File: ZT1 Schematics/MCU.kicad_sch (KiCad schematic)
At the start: 23 parts, among them SW101 PB_WPTKT, U103 74LS02, U106 74LS32, U107 74LS08, U108 74LS00, U111 D444C, U113 2732, U114 2732, U117 P8031AH, U118 74LS373, U127 7432

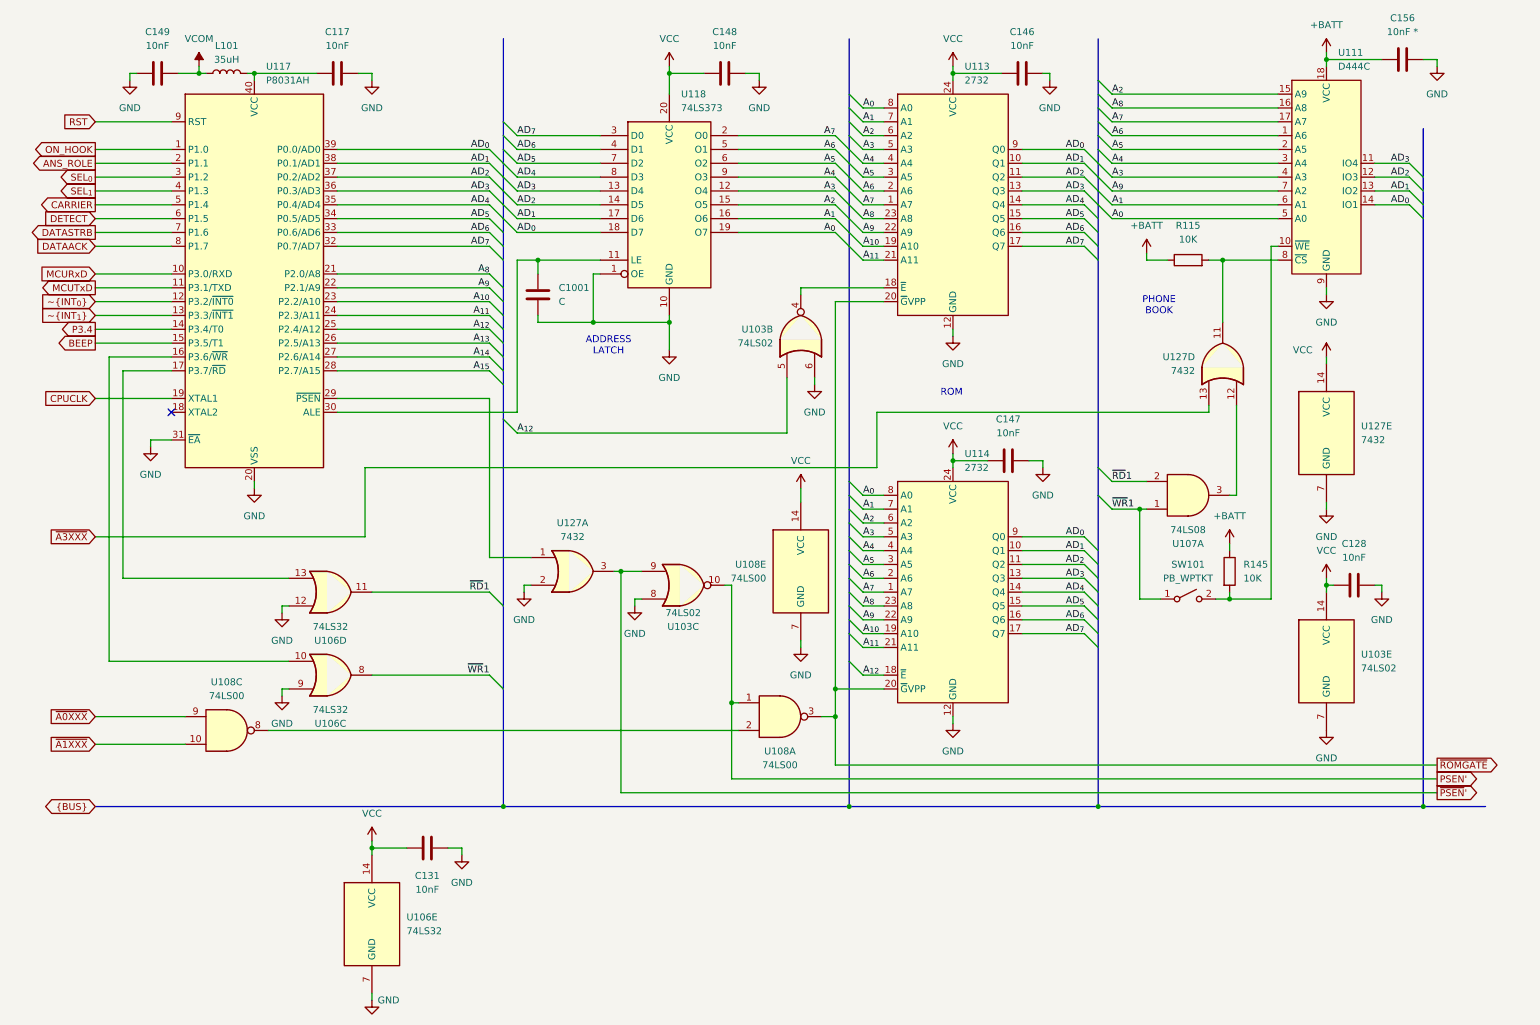
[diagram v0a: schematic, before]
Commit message: Minor touchups
Fixed some of the text
Added some explanations
Simplified the video circuit
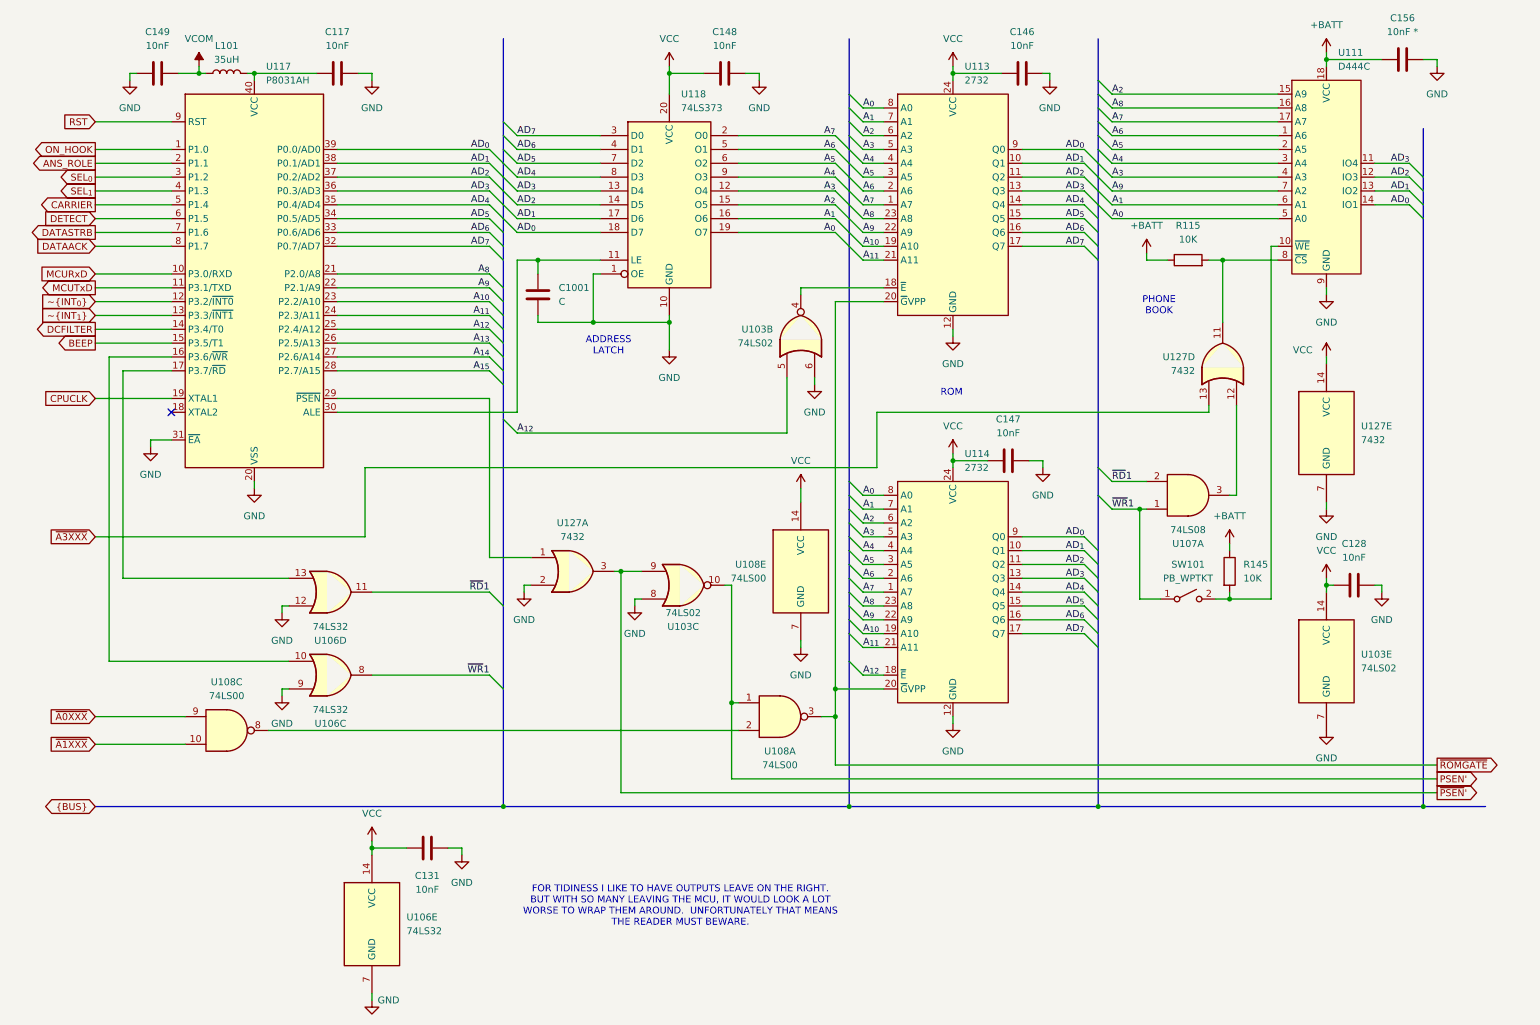
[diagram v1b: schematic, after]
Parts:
- C1001: footprint ZX1:C_Disc_P7.62 -> ZT1:C_Disc_P7.62
- C117, C128, C131, C146, C147, C148, C149, C156: footprint ZX1:C_350mil -> ZT1:C_350mil
- L101: footprint ZX1:L_Axial_L7.0mm_D3.3mm_P5.08mm_Vertical_Fastron_MICC -> ZT1:L_Axial_L7.0mm_D3.3mm_P5.08mm_Vertical_Fastron_MICC
- R115, R145: footprint ZX1:R_450mil -> ZT1:R_450mil
- SW101: footprint ZX1:SW_DIP_SPSTx01_Slide_6.7x4.1mm_W7.62mm_P2.54mm_LowProfile -> ZT1:SW_DIP_SPSTx01_Slide_6.7x4.1mm_W7.62mm_P2.54mm_LowProfile
- U111: symbol ZX1:D444C -> ZT1:D444C
- U113, U114: symbol ZX1:2732 -> ZT1:2732
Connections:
- net P3.4 renamed DCFILTER
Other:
- note added: "FOR TIDINESS I LIKE TO HAVE OUTPUTS LEAVE ON THE RIGHT. BUT WITH SO MANY LEAVING THE MCU, IT WOULD LOOK A LOT WORSE TO WRAP THEM AROUND. UNFORTUNATELY THAT MEANS THE READER MUST BEWARE."
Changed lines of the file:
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@@
 		)
 	)
+	(text "FOR TIDINESS I LIKE TO HAVE OUTPUTS LEAVE ON THE RIGHT.\nBUT WITH SO MANY LEAVING THE MCU, IT WOULD LOOK A LOT\nWORSE TO WRAP THEM AROUND.  UNFORTUNATELY THAT MEANS\nTHE READER MUST BEWARE."
+		(exclude_from_sim no)
+		(at 134.112 177.038 0)
+		(effects
+			(font
+				(size 1.27 1.27)
+			)
+		)
+	)
 	(text "ROM"
 		(exclude_from_sim no)
@@
 		)
 	)
-	(global_label "P3.4"
+	(global_label "DCFILTER"
 		(shape output)
 		(at 26.67 71.12 180)
@@
 		)
 		(property "Intersheetrefs" "${INTERSHEET_REFS}"
-			(at 19.391 71.12 0)
+			(at 15.0367 71.12 0)
 			(effects
 				(font
@@
 			)
 		)
-		(property "Footprint" "ZX1:C_350mil"
+		(property "Footprint" "ZT1:C_350mil"
 			(at 74.93 23.1648 0)
 			(effects
@@
 			)
 		)
-		(property "Datasheet" ""
+		(property "Datasheet" "~"
 			(at 71.12 24.13 0)
 			(effects
@@
 			)
 		)
-		(property "Description" ""
+		(property "Description" "Unpolarized capacitor"
 			(at 71.12 24.13 0)
 			(effects
@@
 	)
 	(symbol
-		(lib_id "ZX1:2732")
+		(lib_id "ZT1:2732")
 		(at 184.15 118.11 0)
 		(unit 1)
@@
 		)
 		(instances
-			(project "ZX1"
+			(project "ZT1"
 				(path "/f4096561-d684-4672-ab54-4b1ef20fc4c8/7726fce8-9145-46c4-9521-1f984b48c1bc"
 					(reference "U114")
@@
 			)
 		)
-		(property "Footprint" "ZX1:C_350mil"
+		(property "Footprint" "ZT1:C_350mil"
 			(at 146.05 23.1648 0)
 			(effects
@@
 			)
 		)
-		(property "Datasheet" ""
+		(property "Datasheet" "~"
 			(at 142.24 24.13 0)
 			(effects
@@
 			)
 		)
-		(property "Description" ""
+		(property "Description" "Unpolarized capacitor"
 			(at 142.24 24.13 0)
 			(effects
@@
 			)
 		)
-		(property "Footprint" "ZX1:R_450mil"
+		(property "Footprint" "ZT1:R_450mil"
 			(at 227.33 60.198 90)
 			(effects
@@
 			)
 		)
-		(property "Datasheet" ""
+		(property "Datasheet" "~"
 			(at 227.33 58.42 0)
 			(effects
@@
 			)
 		)
-		(property "Description" ""
+		(property "Description" "Resistor"
 			(at 227.33 58.42 0)
 			(effects
@@
 		)
 		(instances
-			(project "ZX1"
+			(project "ZT1"
 				(path "/f4096561-d684-4672-ab54-4b1ef20fc4c8/7726fce8-9145-46c4-9521-1f984b48c1bc"
 					(reference "U103")
@@
 		)
 		(instances
-			(project "ZX1"
+			(project "ZT1"
 				(path "/f4096561-d684-4672-ab54-4b1ef20fc4c8/7726fce8-9145-46c4-9521-1f984b48c1bc"
 					(reference "U108")
@@
 		)
 		(instances
-			(project "ZX1"
+			(project "ZT1"
 				(path "/f4096561-d684-4672-ab54-4b1ef20fc4c8/7726fce8-9145-46c4-9521-1f984b48c1bc"
 					(reference "U127")
@@
 			)
 		)
-		(property "Footprint" "ZX1:C_350mil"
+		(property "Footprint" "ZT1:C_350mil"
 			(at 261.62 117.1448 0)
 			(effects
@@
 			)
 		)
-		(property "Datasheet" ""
+		(property "Datasheet" "~"
 			(at 257.81 118.11 0)
 			(effects
@@
 			)
 		)
-		(property "Description" ""
+		(property "Description" "Unpolarized capacitor"
 			(at 257.81 118.11 0)
 			(effects
@@
 	)
 	(symbol
-		(lib_id "ZX1:D444C")
+		(lib_id "ZT1:D444C")
 		(at 252.73 43.18 0)
 		(unit 1)
@@
 		)
 		(instances
-			(project "ZX1"
+			(project "ZT1"
 				(path "/f4096561-d684-4672-ab54-4b1ef20fc4c8/7726fce8-9145-46c4-9521-1f984b48c1bc"
 					(reference "U111")
@@
 		)
 		(instances
-			(project "ZX1"
+			(project "ZT1"
 				(path "/f4096561-d684-4672-ab54-4b1ef20fc4c8/7726fce8-9145-46c4-9521-1f984b48c1bc"
 					(reference "U107")
@@
 			)
 		)
-		(property "Footprint" "ZX1:C_350mil"
+		(property "Footprint" "ZT1:C_350mil"
 			(at 200.66 23.1648 0)
 			(effects
@@
 			)
 		)
-		(property "Datasheet" ""
+		(property "Datasheet" "~"
 			(at 196.85 24.13 0)
 			(effects
@@
 			)
 		)
-		(property "Description" ""
+		(property "Description" "Unpolarized capacitor"
 			(at 196.85 24.13 0)
 			(effects
@@
 		)
 		(instances
-			(project "ZX1"
+			(project "ZT1"
 				(path "/f4096561-d684-4672-ab54-4b1ef20fc4c8/7726fce8-9145-46c4-9521-1f984b48c1bc"
 					(reference "U108")
@@
 		)
 		(instances
-			(project "ZX1"
+			(project "ZT1"
 				(path "/f4096561-d684-4672-ab54-4b1ef20fc4c8/7726fce8-9145-46c4-9521-1f984b48c1bc"
 					(reference "#PWR052")
@@
 		)
 		(instances
-			(project "ZX1"
+			(project "ZT1"
 				(path "/f4096561-d684-4672-ab54-4b1ef20fc4c8/7726fce8-9145-46c4-9521-1f984b48c1bc"
 					(reference "U127")
@@
 			)
 		)
-		(property "Footprint" "ZX1:C_350mil"
+		(property "Footprint" "ZT1:C_350mil"
 			(at 270.51 20.6248 0)
 			(effects
@@
 			)
 		)
-		(property "Datasheet" ""
+		(property "Datasheet" "~"
 			(at 266.7 21.59 0)
 			(effects
@@
 			)
 		)
-		(property "Description" ""
+		(property "Description" "Unpolarized capacitor"
 			(at 266.7 21.59 0)
 			(effects
@@
 		)
 		(instances
-			(project "ZX1"
+			(project "ZT1"
 				(path "/f4096561-d684-4672-ab54-4b1ef20fc4c8/7726fce8-9145-46c4-9521-1f984b48c1bc"
 					(reference "#PWR053")
@@
 			)
 		)
-		(property "Footprint" "ZX1:L_Axial_L7.0mm_D3.3mm_P5.08mm_Vertical_Fastron_MICC"
+		(property "Footprint" "ZT1:L_Axial_L7.0mm_D3.3mm_P5.08mm_Vertical_Fastron_MICC"
 			(at 50.8 24.13 0)
 			(effects
@@
 			)
 		)
-		(property "Datasheet" ""
+		(property "Datasheet" "~"
 			(at 50.8 24.13 0)
 			(effects
@@
 			)
 		)
-		(property "Description" ""
+		(property "Description" "Inductor"
 			(at 50.8 24.13 0)
 			(effects
@@
 		)
 		(instances
-			(project "ZX1"
+			(project "ZT1"
 				(path "/f4096561-d684-4672-ab54-4b1ef20fc4c8/7726fce8-9145-46c4-9521-1f984b48c1bc"
 					(reference "U103")
@@
 			)
 		)
-		(property "Footprint" "ZX1:R_450mil"
+		(property "Footprint" "ZT1:R_450mil"
 			(at 233.172 115.57 90)
 			(effects
@@
 			)
 		)
-		(property "Datasheet" ""
+		(property "Datasheet" "~"
 			(at 234.95 115.57 0)
 			(effects
@@
 			)
 		)
-		(property "Description" ""
+		(property "Description" "Resistor"
 			(at 234.95 115.57 0)
 			(effects
@@
 		)
 		(instances
-			(project "ZX1"
+			(project "ZT1"
 				(path "/f4096561-d684-4672-ab54-4b1ef20fc4c8/7726fce8-9145-46c4-9521-1f984b48c1bc"
 					(reference "R145")
@@
 			)
 		)
-		(property "Footprint" "ZX1:C_350mil"
+		(property "Footprint" "ZT1:C_350mil"
 			(at 198.12 94.2848 0)
 			(effects
@@
 			)
 		)
-		(property "Datasheet" ""
+		(property "Datasheet" "~"
 			(at 194.31 95.25 0)
 			(effects
@@
 			)
 		)
-		(property "Description" ""
+		(property "Description" "Unpolarized capacitor"
 			(at 194.31 95.25 0)
 			(effects
@@
 			)
 		)
-		(property "Footprint" "ZX1:C_350mil"
+		(property "Footprint" "ZT1:C_350mil"
 			(at 41.91 23.1648 0)
 			(effects
@@
 			)
 		)
-		(property "Datasheet" ""
+		(property "Datasheet" "~"
 			(at 38.1 24.13 0)
 			(effects
@@
 			)
 		)
-		(property "Description" ""
+		(property "Description" "Unpolarized capacitor"
 			(at 38.1 24.13 0)
 			(effects
@@
 		)
 		(instances
-			(project "ZX1"
+			(project "ZT1"
 				(path "/f4096561-d684-4672-ab54-4b1ef20fc4c8/7726fce8-9145-46c4-9521-1f984b48c1bc"
 					(reference "#PWR025")
@@
 		)
 		(instances
-			(project "ZX1"
+			(project "ZT1"
 				(path "/f4096561-d684-4672-ab54-4b1ef20fc4c8/7726fce8-9145-46c4-9521-1f984b48c1bc"
 					(reference "#PWR026")
@@
 	)
 	(symbol
-		(lib_id "ZX1:2732")
+		(lib_id "ZT1:2732")
 		(at 184.15 46.99 0)
 		(unit 1)
@@
 		)
 		(instances
-			(project "ZX1"
+			(project "ZT1"
 				(path "/f4096561-d684-4672-ab54-4b1ef20fc4c8/7726fce8-9145-46c4-9521-1f984b48c1bc"
 					(reference "U106")
@@
 		)
 		(instances
-			(project "ZX1"
+			(project "ZT1"
 				(path "/f4096561-d684-4672-ab54-4b1ef20fc4c8/7726fce8-9145-46c4-9521-1f984b48c1bc"
 					(reference "U103")
@@
 		)
 		(instances
-			(project "ZX1"
+			(project "ZT1"
 				(path "/f4096561-d684-4672-ab54-4b1ef20fc4c8/7726fce8-9145-46c4-9521-1f984b48c1bc"
 					(reference "U106")
@@
 		)
 		(instances
-			(project "ZX1"
+			(project "ZT1"
 				(path "/f4096561-d684-4672-ab54-4b1ef20fc4c8/7726fce8-9145-46c4-9521-1f984b48c1bc"
 					(reference "U127")
@@
 			)
 		)
-		(property "Footprint" "ZX1:C_350mil"
+		(property "Footprint" "ZT1:C_350mil"
 			(at 91.44 165.4048 0)
 			(effects
@@
 			)
 		)
-		(property "Datasheet" ""
+		(property "Datasheet" "~"
 			(at 87.63 166.37 0)
 			(effects
@@
 			)
 		)
-		(property "Description" ""
+		(property "Description" "Unpolarized capacitor"
 			(at 87.63 166.37 0)
 			(effects
@@
 		)
 		(instances
-			(project "ZX1"
+			(project "ZT1"
 				(path "/f4096561-d684-4672-ab54-4b1ef20fc4c8/7726fce8-9145-46c4-9521-1f984b48c1bc"
 					(reference "#PWR01006")
@@
 		)
 		(instances
-			(project "ZX1"
+			(project "ZT1"
 				(path "/f4096561-d684-4672-ab54-4b1ef20fc4c8/7726fce8-9145-46c4-9521-1f984b48c1bc"
 					(reference "U106")
@@
 		)
 		(instances
-			(project "ZX1"
+			(project "ZT1"
 				(path "/f4096561-d684-4672-ab54-4b1ef20fc4c8/7726fce8-9145-46c4-9521-1f984b48c1bc"
 					(reference "U108")
@@
 			)
 		)
-		(property "Footprint" "ZX1:SW_DIP_SPSTx01_Slide_6.7x4.1mm_W7.62mm_P2.54mm_LowProfile"
+		(property "Footprint" "ZT1:SW_DIP_SPSTx01_Slide_6.7x4.1mm_W7.62mm_P2.54mm_LowProfile"
 			(at 227.33 120.65 0)
 			(effects
@@
 		)
 		(instances
-			(project "ZX1"
+			(project "ZT1"
 				(path "/f4096561-d684-4672-ab54-4b1ef20fc4c8/7726fce8-9145-46c4-9521-1f984b48c1bc"
 					(reference "SW101")
@@
 			)
 		)
-		(property "Footprint" "ZX1:C_Disc_P7.62"
+		(property "Footprint" "ZT1:C_Disc_P7.62"
 			(at 108.9152 68.58 0)
 			(effects
@@
 			)
 		)
-		(property "Datasheet" ""
+		(property "Datasheet" "~"
 			(at 107.95 64.77 0)
 			(effects
@@
 			)
 		)
-		(property "Description" ""
+		(property "Description" "Unpolarized capacitor"
 			(at 107.95 64.77 0)
 			(effects
